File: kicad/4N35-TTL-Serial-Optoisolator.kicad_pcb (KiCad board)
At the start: 2 copper layers, 40.6 x 22.9 mm, 17 parts, among them P1 CONN_4, P2 CONN_4, Q1 2N3906, Q2 2N3906, U1 4N35, U2 4N35

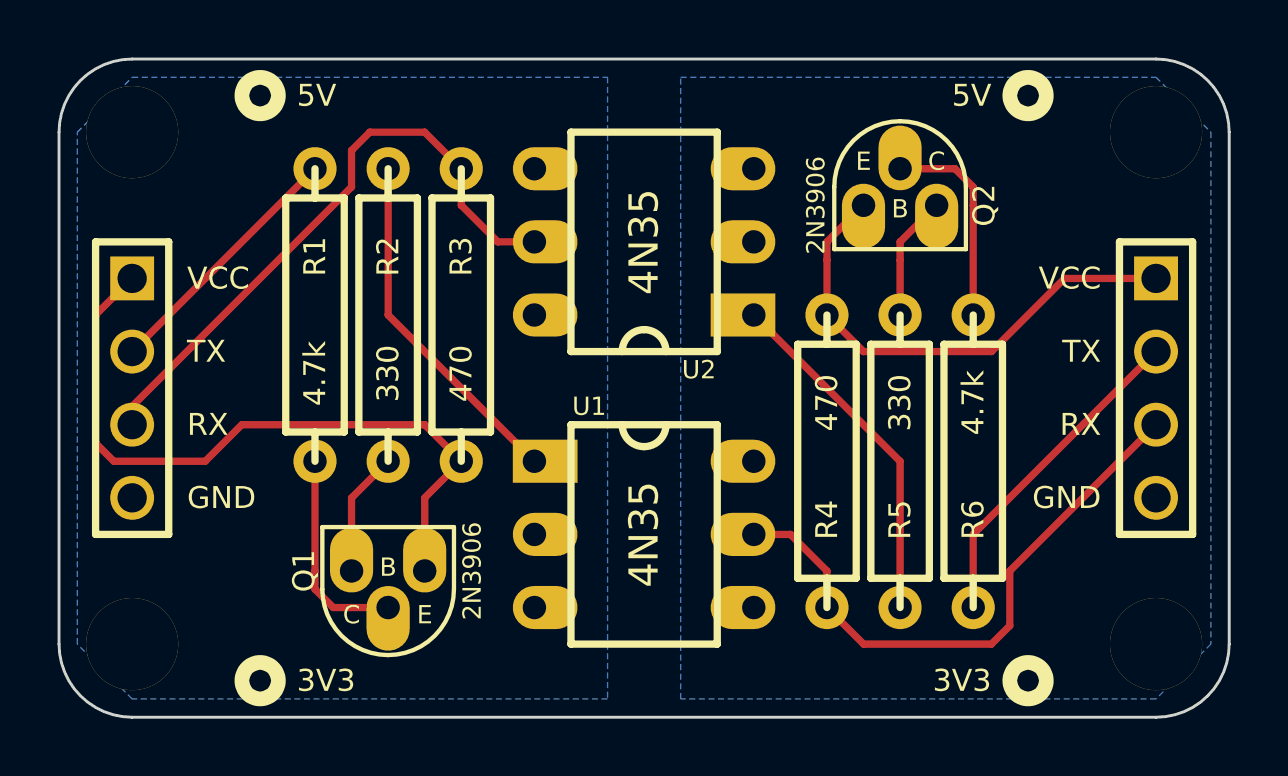
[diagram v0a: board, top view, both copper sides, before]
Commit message: fattening traces to 20 mil
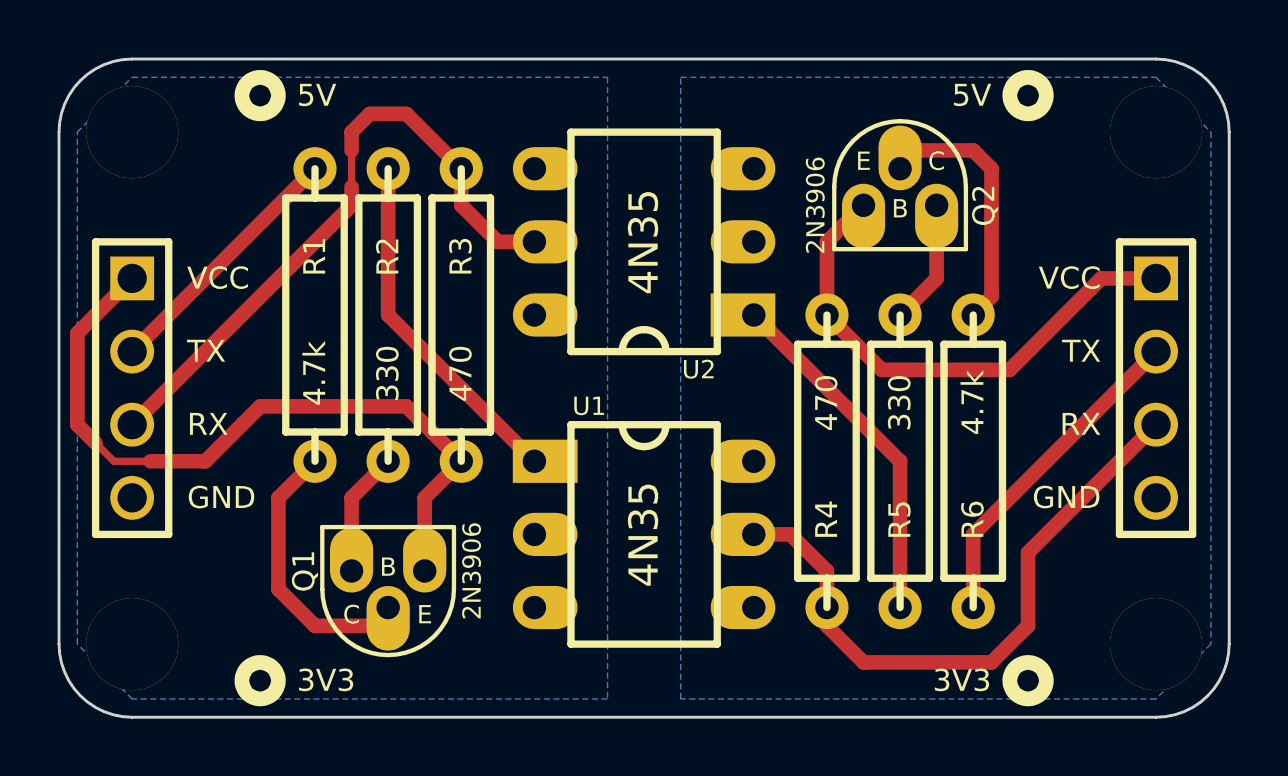
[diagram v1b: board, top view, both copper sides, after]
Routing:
- net N-0000012: track 7.25 -> 9.57 mm
- net N-000005: track 7.25 -> 9.04 mm
- net RXB: track 20.6 -> 21.8 mm
- net VCCA: track 24.6 -> 25.6 mm
- net RXA: track 21.6 -> 22.5 mm
- net VCCB: track 17.3 -> 17.9 mm

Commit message: fixing silkscreen text
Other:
- board text added: "4N35 TTL Serial Optoisolator v1"
- board text removed: "TTL Serial Optoisolator v1"
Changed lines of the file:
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@@
   )
   (setup
-    (last_trace_width 0.508)
+    (last_trace_width 0.254)
     (user_trace_width 0.508)
     (trace_clearance 0.254)
@@
     (effects (font (size 0.635 0.635) (thickness 0.127)) (justify mirror))
   )
-  (gr_text "TTL Serial Optoisolator v1" (at 219.71 53.34) (layer B.SilkS)
+  (gr_text "4N35 TTL Serial Optoisolator v1" (at 219.71 53.34) (layer B.SilkS)
     (effects (font (size 1.016 1.016) (thickness 0.2032)) (justify mirror))
   )
@@
   (segment (start 210.82 66.04) (end 209.55 67.31) (width 0.508) (layer F.Cu) (net 3))
   (segment (start 209.55 67.31) (end 209.55 69.85) (width 0.508) (layer F.Cu) (net 3))
-  (segment (start 208.28 66.04) (end 207.01 67.31) (width 0.508) (layer F.Cu) (net 4) (status 400000))
-  (segment (start 210.185 71.755) (end 210.82 71.12) (width 0.508) (layer F.Cu) (net 4) (status C00000))
-  (segment (start 208.28 71.755) (end 210.185 71.755) (width 0.508) (layer F.Cu) (net 4) (status 800000))
+  (segment (start 208.28 66.04) (end 207.01 67.31) (width 0.508) (layer F.Cu) (net 4))
+  (segment (start 210.185 71.755) (end 210.82 71.12) (width 0.508) (layer F.Cu) (net 4))
+  (segment (start 208.28 71.755) (end 210.185 71.755) (width 0.508) (layer F.Cu) (net 4))
   (segment (start 207.01 70.485) (end 208.28 71.755) (width 0.508) (layer F.Cu) (net 4))
   (segment (start 207.01 67.31) (end 207.01 70.485) (width 0.508) (layer F.Cu) (net 4))
   (segment (start 210.82 55.88) (end 210.82 60.96) (width 0.508) (layer F.Cu) (net 5))
   (segment (start 210.82 60.96) (end 215.9 66.04) (width 0.508) (layer F.Cu) (net 5))
-  (segment (start 231.14 60.96) (end 231.775 60.325) (width 0.508) (layer F.Cu) (net 6) (status C00000))
-  (segment (start 229.235 55.245) (end 228.6 55.88) (width 0.508) (layer F.Cu) (net 6) (status C00000))
-  (segment (start 231.14 55.245) (end 229.235 55.245) (width 0.508) (layer F.Cu) (net 6) (status 800000))
+  (segment (start 231.14 60.96) (end 231.775 60.325) (width 0.508) (layer F.Cu) (net 6))
+  (segment (start 229.235 55.245) (end 228.6 55.88) (width 0.508) (layer F.Cu) (net 6))
+  (segment (start 231.14 55.245) (end 229.235 55.245) (width 0.508) (layer F.Cu) (net 6))
   (segment (start 231.775 55.88) (end 231.14 55.245) (width 0.508) (layer F.Cu) (net 6))
-  (segment (start 231.775 60.325) (end 231.775 55.88) (width 0.508) (layer F.Cu) (net 6) (status 400000))
-  (segment (start 228.6 60.96) (end 229.87 59.69) (width 0.508) (layer F.Cu) (net 7) (status 400000))
-  (segment (start 229.87 59.69) (end 229.87 57.15) (width 0.508) (layer F.Cu) (net 7) (status 800000))
+  (segment (start 231.775 60.325) (end 231.775 55.88) (width 0.508) (layer F.Cu) (net 6))
+  (segment (start 228.6 60.96) (end 229.87 59.69) (width 0.508) (layer F.Cu) (net 7))
+  (segment (start 229.87 59.69) (end 229.87 57.15) (width 0.508) (layer F.Cu) (net 7))
   (segment (start 223.52 60.96) (end 228.6 66.04) (width 0.508) (layer F.Cu) (net 8))
   (segment (start 228.6 66.04) (end 228.6 71.12) (width 0.508) (layer F.Cu) (net 8))
   (segment (start 209.55 55.245) (end 209.55 54.61) (width 0.508) (layer F.Cu) (net 9))
-  (segment (start 201.93 64.77) (end 209.55 57.15) (width 0.508) (layer F.Cu) (net 9) (status 400000))
+  (segment (start 201.93 64.77) (end 209.55 57.15) (width 0.508) (layer F.Cu) (net 9))
   (segment (start 209.55 57.15) (end 209.55 56.515) (width 0.508) (layer F.Cu) (net 9))
   (segment (start 209.55 55.245) (end 209.55 56.515) (width 0.254) (layer F.Cu) (net 9))
-  (segment (start 211.455 53.975) (end 213.36 55.88) (width 0.508) (layer F.Cu) (net 9) (status 800000))
+  (segment (start 211.455 53.975) (end 213.36 55.88) (width 0.508) (layer F.Cu) (net 9))
   (segment (start 210.185 53.975) (end 211.455 53.975) (width 0.508) (layer F.Cu) (net 9))
   (segment (start 209.55 54.61) (end 210.185 53.975) (width 0.508) (layer F.Cu) (net 9))
@@
   (segment (start 213.36 57.15) (end 214.63 58.42) (width 0.508) (layer F.Cu) (net 9))
   (segment (start 214.63 58.42) (end 215.9 58.42) (width 0.508) (layer F.Cu) (net 9))
-  (segment (start 226.06 71.12) (end 226.06 71.755) (width 0.508) (layer F.Cu) (net 10) (status C00000))
-  (segment (start 233.045 69.215) (end 237.49 64.77) (width 0.508) (layer F.Cu) (net 10) (status 800000))
+  (segment (start 226.06 71.12) (end 226.06 71.755) (width 0.508) (layer F.Cu) (net 10))
+  (segment (start 233.045 69.215) (end 237.49 64.77) (width 0.508) (layer F.Cu) (net 10))
   (segment (start 233.045 71.755) (end 233.045 69.215) (width 0.508) (layer F.Cu) (net 10))
   (segment (start 231.775 73.025) (end 233.045 71.755) (width 0.508) (layer F.Cu) (net 10))
   (segment (start 227.33 73.025) (end 231.775 73.025) (width 0.508) (layer F.Cu) (net 10))
-  (segment (start 226.06 71.755) (end 227.33 73.025) (width 0.508) (layer F.Cu) (net 10) (status 400000))
+  (segment (start 226.06 71.755) (end 227.33 73.025) (width 0.508) (layer F.Cu) (net 10))
   (segment (start 223.52 68.58) (end 224.79 68.58) (width 0.508) (layer F.Cu) (net 10))
   (segment (start 226.06 69.85) (end 226.06 71.12) (width 0.508) (layer F.Cu) (net 10))
@@
   (segment (start 227.33 62.23) (end 227.965 62.865) (width 0.508) (layer F.Cu) (net 14))
   (segment (start 226.06 60.96) (end 227.33 62.23) (width 0.508) (layer F.Cu) (net 14))
-  (segment (start 235.585 59.69) (end 237.49 59.69) (width 0.508) (layer F.Cu) (net 14) (status 800000))
+  (segment (start 235.585 59.69) (end 237.49 59.69) (width 0.508) (layer F.Cu) (net 14))
   (segment (start 232.41 62.865) (end 235.585 59.69) (width 0.508) (layer F.Cu) (net 14))
   (segment (start 227.965 62.865) (end 232.41 62.865) (width 0.508) (layer F.Cu) (net 14))
-  (segment (start 226.06 60.96) (end 226.06 58.42) (width 0.508) (layer F.Cu) (net 14) (status 400000))
-  (segment (start 226.06 58.42) (end 227.33 57.15) (width 0.508) (layer F.Cu) (net 14) (status 800000))
+  (segment (start 226.06 60.96) (end 226.06 58.42) (width 0.508) (layer F.Cu) (net 14))
+  (segment (start 226.06 58.42) (end 227.33 57.15) (width 0.508) (layer F.Cu) (net 14))
   (zone (net 1) (net_name GNDA) (layer B.Cu) (hatch edge 0.508)
     (connect_pads (clearance 0.508))
